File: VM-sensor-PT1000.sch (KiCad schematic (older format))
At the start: 17 parts, among them P1 PT100, P2 ADC, P3 PWR, U1 AMS1117, U2 MCP6001

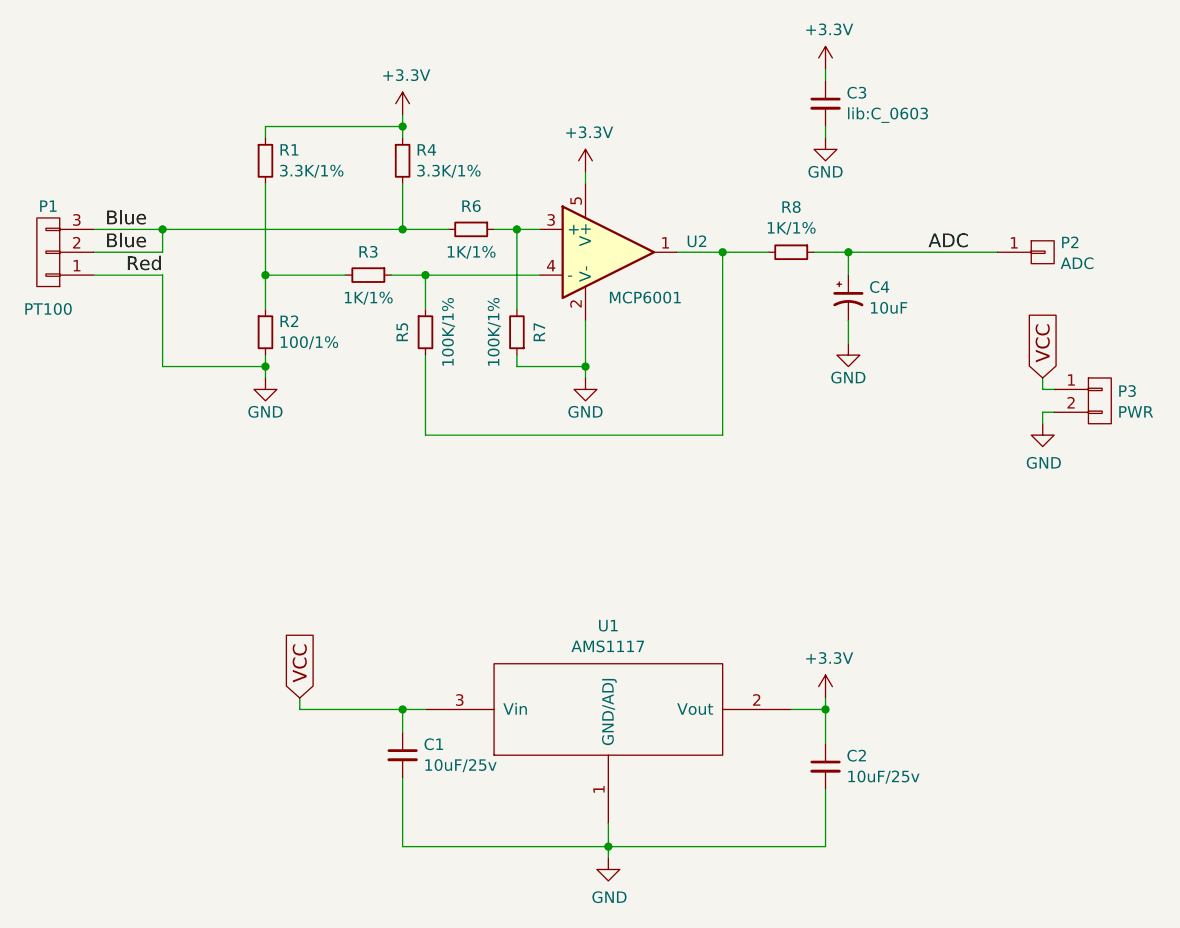
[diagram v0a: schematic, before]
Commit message: Fix value resistor R3,R6, R7, R5 & symbol R2
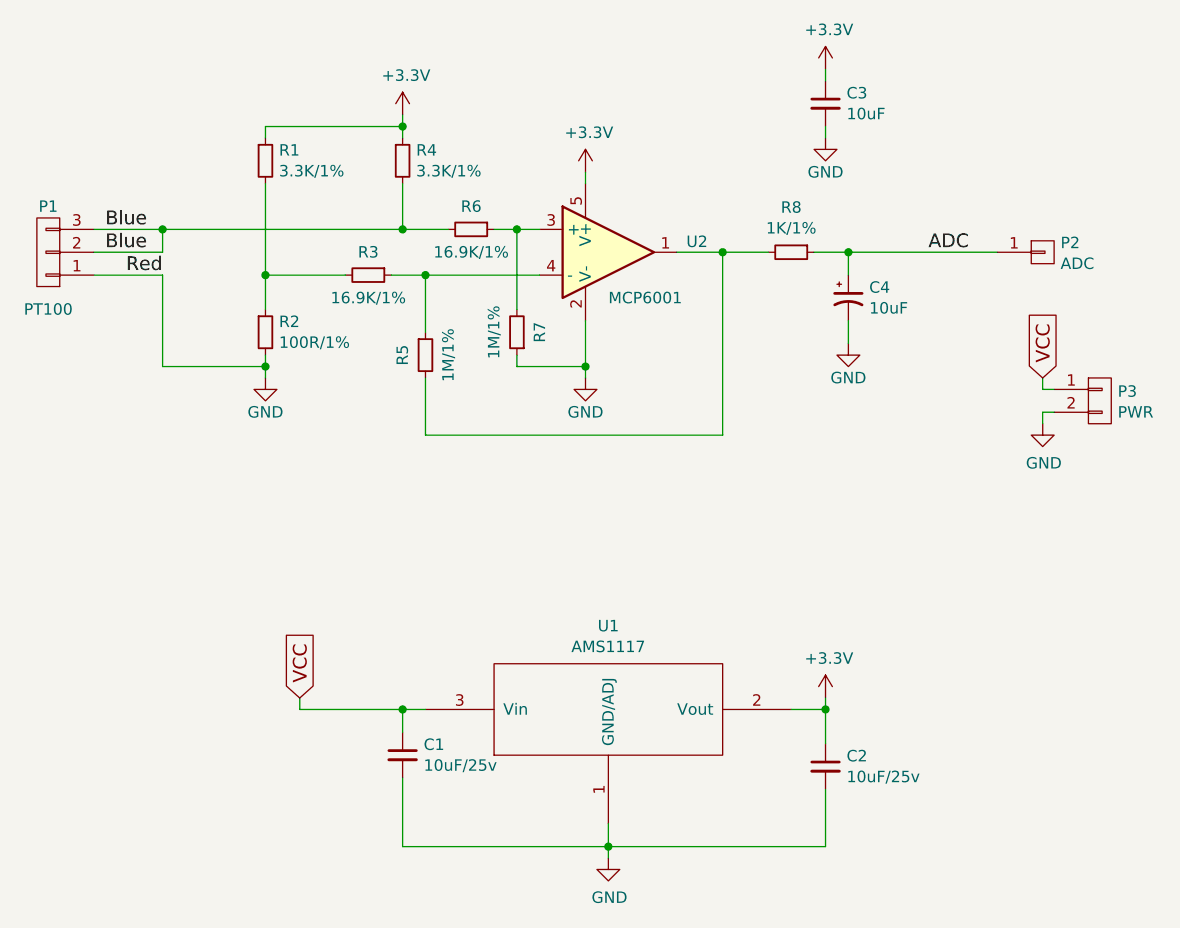
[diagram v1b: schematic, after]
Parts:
- C3: value lib:C_0603 -> 10uF
- R2: value 100/1% -> 100R/1%
- R3, R6: value 1K/1% -> 16.9K/1%
- R5, R7: value 100K/1% -> 1M/1%
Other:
- moved on the sheet: R5
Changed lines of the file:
@@
 LIBS:valves
 LIBS:AMS1117
+LIBS:VM-sensor-PT1000-cache
 EELAYER 26 0
 EELAYER END
@@
 P 5700 3200
 F 0 "R7" V 5600 3200 50  0000 C CNN
-F 1 "100K/1%" V 5800 3200 50  0000 C CNN
+F 1 "1M/1%" V 5800 3200 50  0000 C CNN
 F 2 "Resistors_SMD:R_0805" H 5700 3200 50  0001 C CNN
 F 3 "" H 5700 3200 50  0000 C CNN
@@
 P 4600 3200
 F 0 "R2" H 4659 3246 50  0000 L CNN
-F 1 "100/1%" H 4659 3155 50  0000 L CNN
+F 1 "100R/1%" H 4659 3155 50  0000 L CNN
 F 2 "Resistors_SMD:R_0805" H 4600 3200 50  0001 C CNN
 F 3 "" H 4600 3200 50  0000 C CNN
@@
 P 5050 2950
 F 0 "R3" V 4950 2950 50  0000 C CNN
-F 1 "1K/1%" V 5150 2950 50  0000 C CNN
+F 1 "16.9K/1%" V 5150 2950 50  0000 C CNN
 F 2 "Resistors_SMD:R_0805" H 5050 2950 50  0001 C CNN
 F 3 "" H 5050 2950 50  0000 C CNN
@@
 L R_Small R5
 U 1 1 585E5486
-P 5300 3200
-F 0 "R5" V 5200 3200 50  0000 C CNN
-F 1 "100K/1%" V 5400 3200 50  0000 C CNN
-F 2 "Resistors_SMD:R_0805" H 5300 3200 50  0001 C CNN
-F 3 "" H 5300 3200 50  0000 C CNN
-	1    5300 3200
+P 5300 3300
+F 0 "R5" V 5200 3300 50  0000 C CNN
+F 1 "1M/1%" V 5400 3300 50  0000 C CNN
+F 2 "Resistors_SMD:R_0805" H 5300 3300 50  0001 C CNN
+F 3 "" H 5300 3300 50  0000 C CNN
+	1    5300 3300
 	1    0    0    -1
 $EndComp
@@
 Connection ~ 6600 2850
 Wire Wire Line
-	6000 3400 6000 3150
+	6000 3150 6000 3400
 Wire Wire Line
 	4750 4800 4750 4850
@@
 P 7050 2200
 F 0 "C3" H 7142 2246 50  0000 L CNN
-F 1 "lib:C_0603" H 7142 2155 50  0000 L CNN
+F 1 "10uF" H 7142 2155 50  0000 L CNN
 F 2 "Capacitors_SMD:C_0805" H 7050 2200 50  0001 C CNN
 F 3 "" H 7050 2200 50  0000 C CNN
@@
 P 5500 2750
 F 0 "R6" V 5400 2750 50  0000 C CNN
-F 1 "1K/1%" V 5600 2750 50  0000 C CNN
+F 1 "16.9K/1%" V 5600 2750 50  0000 C CNN
 F 2 "Resistors_SMD:R_0805" H 5500 2750 50  0001 C CNN
 F 3 "" H 5500 2750 50  0000 C CNN
@@
 	5150 2950 5800 2950
 Wire Wire Line
-	5300 2950 5300 3100
+	5300 2950 5300 3200
 Connection ~ 5300 2950
 Wire Wire Line
-	5300 3300 5300 3650
+	5300 3400 5300 3650
 Wire Wire Line
 	5300 3650 6600 3650
